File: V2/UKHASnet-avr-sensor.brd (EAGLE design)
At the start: 49.5 x 49.2 mm, 33 parts, among them J1 AVR_SPI_PRG_62X3_LOCK, U1 MCP1700-3302E/TO, U2 ATMEGA328P-PU, X1 SMA-142-0711-881/886, Y1 RESONATORPTH

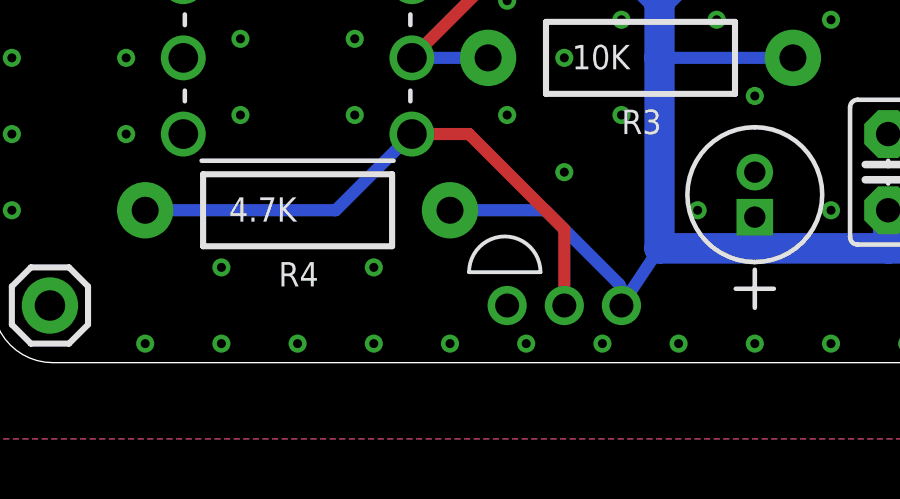
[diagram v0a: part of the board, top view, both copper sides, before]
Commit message: Add extra pad for dht22.
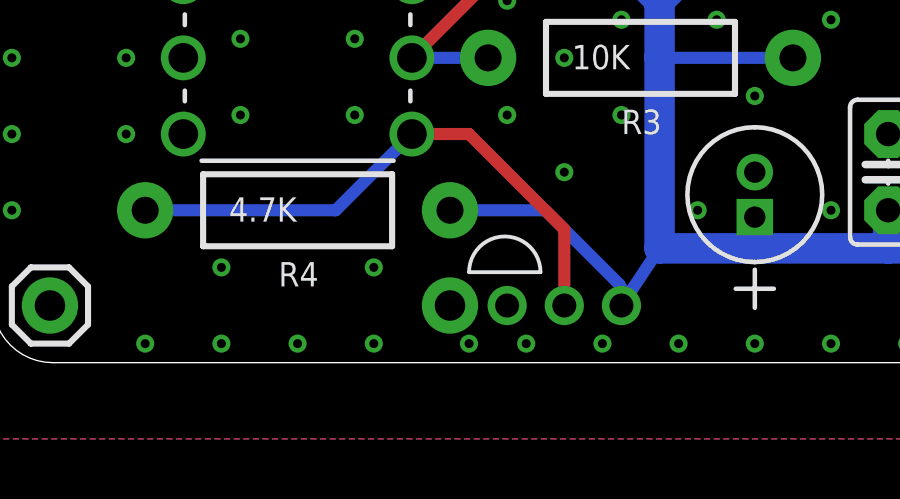
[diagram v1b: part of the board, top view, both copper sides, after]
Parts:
- added JP16: M01NOSILK-KIT, SparkFun-Connectors:1X01NS-KIT
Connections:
- net GND: now also JP16.1
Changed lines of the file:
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@@
 <layer number="54" name="bGND_GNDA" color="1" fill="9" visible="no" active="no"/>
 <layer number="56" name="wert" color="7" fill="1" visible="no" active="no"/>
+<layer number="57" name="tCAD" color="7" fill="1" visible="no" active="no"/>
 <layer number="91" name="Nets" color="2" fill="1" visible="no" active="no"/>
 <layer number="92" name="Busses" color="1" fill="1" visible="no" active="no"/>
@@
 <layer number="97" name="Info" color="7" fill="1" visible="no" active="no"/>
 <layer number="98" name="Guide" color="6" fill="1" visible="no" active="no"/>
+<layer number="99" name="SpiceOrder" color="7" fill="1" visible="no" active="no"/>
 <layer number="100" name="Muster" color="7" fill="1" visible="no" active="no"/>
 <layer number="101" name="Patch_Top" color="12" fill="4" visible="no" active="yes"/>
@@
 <layer number="109" name="fp9" color="7" fill="1" visible="no" active="yes"/>
 <layer number="110" name="fp0" color="7" fill="1" visible="no" active="yes"/>
+<layer number="111" name="LPC17xx" color="7" fill="1" visible="no" active="yes"/>
+<layer number="112" name="tSilk" color="7" fill="1" visible="no" active="yes"/>
+<layer number="113" name="IDFDebug" color="4" fill="1" visible="no" active="yes"/>
 <layer number="116" name="Patch_BOT" color="9" fill="4" visible="no" active="yes"/>
 <layer number="121" name="_tsilk" color="7" fill="1" visible="no" active="yes"/>
@@
 <layer number="124" name="bTestmark" color="7" fill="1" visible="no" active="yes"/>
 <layer number="125" name="_tNames" color="7" fill="1" visible="no" active="yes"/>
+<layer number="126" name="_bNames" color="7" fill="1" visible="no" active="yes"/>
+<layer number="127" name="_tValues" color="7" fill="1" visible="no" active="yes"/>
+<layer number="128" name="_bValues" color="7" fill="1" visible="no" active="yes"/>
 <layer number="131" name="tAdjust" color="7" fill="1" visible="no" active="yes"/>
 <layer number="132" name="bAdjust" color="7" fill="1" visible="no" active="yes"/>
 <layer number="144" name="Drill_legend" color="7" fill="1" visible="no" active="yes"/>
+<layer number="150" name="Notes" color="7" fill="1" visible="no" active="yes"/>
 <layer number="151" name="HeatSink" color="7" fill="1" visible="no" active="yes"/>
+<layer number="152" name="_bDocu" color="7" fill="1" visible="no" active="yes"/>
+<layer number="153" name="FabDoc1" color="7" fill="1" visible="no" active="yes"/>
+<layer number="154" name="FabDoc2" color="7" fill="1" visible="no" active="yes"/>
+<layer number="155" name="FabDoc3" color="7" fill="1" visible="no" active="yes"/>
 <layer number="199" name="Contour" color="7" fill="1" visible="no" active="yes"/>
 <layer number="200" name="200bmp" color="1" fill="10" visible="no" active="no"/>
@@
 <layer number="223" name="223bmp" color="24" fill="1" visible="no" active="no"/>
 <layer number="224" name="224bmp" color="25" fill="1" visible="no" active="no"/>
+<layer number="248" name="Housing" color="7" fill="1" visible="no" active="yes"/>
+<layer number="249" name="Edge" color="7" fill="1" visible="no" active="yes"/>
 <layer number="250" name="Descript" color="3" fill="1" visible="no" active="no"/>
 <layer number="251" name="SMDround" color="12" fill="11" visible="no" active="no"/>
@@
 <element name="JP15" library="SparkFun-Connectors" package="1X01" value="M01PTH" x="1.905" y="31.75" smashed="yes"/>
 <element name="U$3" library="SparkFun-Aesthetics" package="OSHW-LOGO-M" value="" x="45.72" y="8.89" rot="R90"/>
+<element name="JP16" library="SparkFun-Connectors" package="1X01NS-KIT" value="M01NOSILK-KIT" x="15.24" y="1.905"/>
 </elements>
 <signals>
@@
 <via x="10.16" y="0.635" extent="1-16" drill="0.3"/>
 <via x="12.7" y="0.635" extent="1-16" drill="0.3"/>
-<via x="15.24" y="0.635" extent="1-16" drill="0.3"/>
+<via x="15.875" y="0.635" extent="1-16" drill="0.3"/>
 <via x="17.78" y="0.635" extent="1-16" drill="0.3"/>
 <via x="20.32" y="0.635" extent="1-16" drill="0.3"/>
@@
 <via x="47.625" y="45.085" extent="1-16" drill="0.3"/>
 <via x="43.18" y="43.18" extent="1-16" drill="0.3"/>
+<contactref element="JP16" pad="1"/>
 </signal>
 <signal name="VIN">

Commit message: Fix dht22 pad.
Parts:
- removed JP16: M01NOSILK-KIT, SparkFun-Connectors:1X01NS-KIT
- added PAD1: WIREPAD1,6/0,9, wirepad:1,6/0,9
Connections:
- net GND: now also PAD1.1; no longer JP16.1
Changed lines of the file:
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@@
 <elements>
 <element name="U$1" library="hopeRF2" package="RFM" value="RFM69HW" x="47.625" y="41.91" smashed="yes" rot="R180"/>
-<element name="U$2" library="Ava" package="DS1820" value="DS1820TO92" x="16.51" y="3.175"/>
+<element name="U$2" library="Ava" package="DS1820" value="DS1820TO92" x="16.51" y="3.175" smashed="yes"/>
 <element name="J1" library="SparkFun-Connectors" package="2X3_LOCK" value="AVR_SPI_PRG_62X3_LOCK" x="44.45" y="19.05" smashed="yes" rot="R270"/>
 <element name="JP1" library="SparkFun-Connectors" package="1X02" value="M02PTH" x="47.625" y="1.905" smashed="yes" rot="R180"/>
@@
 <element name="JP15" library="SparkFun-Connectors" package="1X01" value="M01PTH" x="1.905" y="31.75" smashed="yes"/>
 <element name="U$3" library="SparkFun-Aesthetics" package="OSHW-LOGO-M" value="" x="45.72" y="8.89" rot="R90"/>
-<element name="JP16" library="SparkFun-Connectors" package="1X01NS-KIT" value="M01NOSILK-KIT" x="15.24" y="1.905"/>
+<element name="PAD1" library="wirepad" package="1,6/0,9" value="WIREPAD1,6/0,9" x="15.24" y="1.905" smashed="yes"/>
 </elements>
 <signals>
@@
 <via x="47.625" y="45.085" extent="1-16" drill="0.3"/>
 <via x="43.18" y="43.18" extent="1-16" drill="0.3"/>
-<contactref element="JP16" pad="1"/>
+<contactref element="PAD1" pad="1"/>
 </signal>
 <signal name="VIN">

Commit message: Silkscreen changes.
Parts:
- C1: value 47UF -> 47uF
- C4, C5, C6: value 100nF -> 0.1uF
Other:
- board text added: "https://ukhas.net/"
- board text removed: "http://ukhas.net/"
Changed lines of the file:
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@@
 <wire x1="2" y1="49.2" x2="0" y2="47.2" width="0" layer="20" curve="90"/>
 <text x="41.91" y="10.16" size="1.778" layer="51" distance="96" rot="R90">Phil M0DNY</text>
-<text x="24.13" y="12.7" size="1.778" layer="51" rot="R90">http://ukhas.net/</text>
+<text x="24.765" y="12.7" size="1.778" layer="51" rot="R90">https://ukhas.net/</text>
 <text x="41.91" y="1.27" size="1.9304" layer="51">+</text>
 <text x="36.83" y="10.16" size="1.778" layer="51" rot="R90">Sensor V2</text>
@@
 <element name="JP9" library="SparkFun-Connectors" package="1X01" value="M01PTH" x="24.765" y="46.355" smashed="yes"/>
 <element name="R1" library="SparkFun" package="AXIAL-0.4" value="150K" x="27.305" y="19.05" smashed="yes" rot="R90">
-<attribute name="NAME" x="26.035" y="14.605" size="0.8128" layer="25" font="vector" ratio="15" rot="R90"/>
+<attribute name="NAME" x="29.21" y="13.97" size="0.8128" layer="25" font="vector" ratio="15" rot="R90"/>
 <attribute name="VALUE" x="27.686" y="16.764" size="0.8128" layer="21" font="vector" ratio="15" rot="R90"/>
 </element>
 <element name="R2" library="SparkFun" package="AXIAL-0.4" value="470K" x="31.115" y="19.05" smashed="yes" rot="R270">
-<attribute name="NAME" x="29.21" y="15.875" size="0.8128" layer="25" font="vector" ratio="15" rot="R270"/>
+<attribute name="NAME" x="32.385" y="15.24" size="0.8128" layer="25" font="vector" ratio="15" rot="R270"/>
 <attribute name="VALUE" x="30.734" y="19.431" size="0.8128" layer="21" font="vector" ratio="15" rot="R270"/>
 </element>
@@
 <attribute name="VALUE" x="19.304" y="9.779" size="0.8128" layer="21" font="vector" ratio="15"/>
 </element>
-<element name="C1" library="1000ufCap" package="CAPPR150-400X1200" value="47UF" x="25.4" y="6.35" smashed="yes" rot="R90">
+<element name="C1" library="1000ufCap" package="CAPPR150-400X1200" value="47uF" x="25.4" y="6.35" smashed="yes" rot="R90">
 <attribute name="OC_NEWARK" value="17T5110 " x="25.4" y="6.35" size="1.778" layer="27" rot="R90" display="off"/>
 <attribute name="TOLERANCE" value="±20 %" x="25.4" y="6.35" size="1.778" layer="27" rot="R90" display="off"/>
@@
 <attribute name="SUPPLIER" value="PANASONIC " x="25.4" y="6.35" size="1.778" layer="27" rot="R90" display="off"/>
 <attribute name="OC_FARNELL" value="1848468 " x="25.4" y="6.35" size="1.778" layer="27" rot="R90" display="off"/>
+<attribute name="VALUE" x="19.7358" y="4.9784" size="0.8128" layer="27" font="vector" ratio="15" rot="SR0"/>
 </element>
 <element name="R4" library="SparkFun" package="AXIAL-0.4" value="4.7K" x="10.16" y="5.08" smashed="yes">
@@
 <element name="C2" library="capacitor-wima" package="C2.5-2" value="100nF" x="17.78" y="24.765" smashed="yes" rot="R90"/>
 <element name="C3" library="capacitor-wima" package="C2.5-2" value="100nF" x="17.78" y="29.845" smashed="yes" rot="R90"/>
-<element name="C4" library="capacitor-wima" package="C2.5-2" value="100nF" x="39.37" y="6.35" smashed="yes" rot="R90"/>
-<element name="C6" library="capacitor-wima" package="C2.5-2" value="100nF" x="29.845" y="6.35" smashed="yes" rot="R90"/>
-<element name="C5" library="capacitor-wima" package="C2.5-2" value="100nF" x="46.355" y="43.18" smashed="yes" rot="R180"/>
+<element name="C4" library="capacitor-wima" package="C2.5-2" value="0.1uF" x="39.37" y="6.35" smashed="yes" rot="R90">
+<attribute name="VALUE" x="41.021" y="3.429" size="0.8128" layer="27" font="vector" ratio="15" rot="R180"/>
+</element>
+<element name="C6" library="capacitor-wima" package="C2.5-2" value="0.1uF" x="29.845" y="6.35" smashed="yes" rot="R90">
+<attribute name="VALUE" x="31.496" y="3.429" size="0.8128" layer="27" font="vector" ratio="15" rot="R180"/>
+</element>
+<element name="C5" library="capacitor-wima" package="C2.5-2" value="0.1uF" x="46.355" y="43.18" smashed="yes" rot="R180">
+<attribute name="VALUE" x="46.736" y="45.974" size="0.8128" layer="27" font="vector" ratio="15" rot="R180"/>
+</element>
 <element name="JP5" library="SparkFun-Connectors" package="1X01" value="M01PTH" x="1.905" y="28.575" smashed="yes"/>
 <element name="JP6" library="SparkFun-Connectors" package="1X01" value="M01PTH" x="1.905" y="26.035" smashed="yes"/>

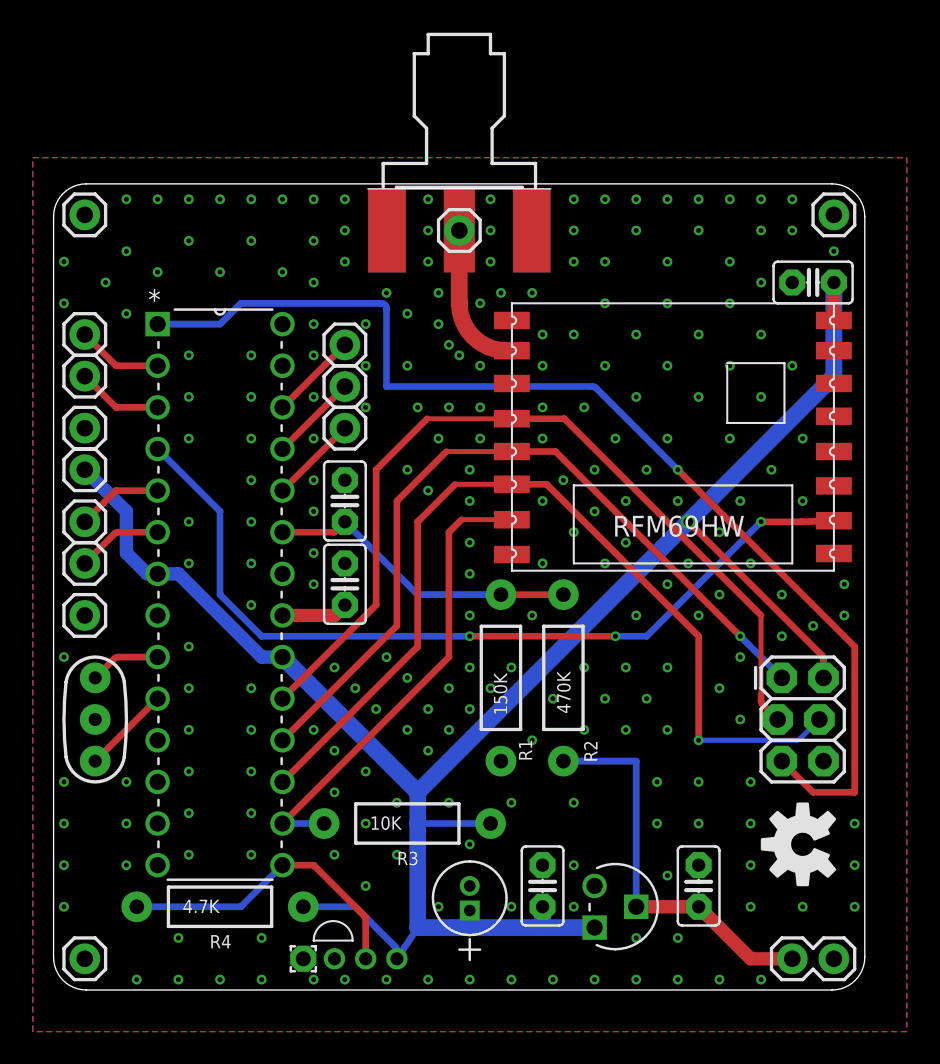
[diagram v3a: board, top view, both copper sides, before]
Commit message: Silkscreen changes.
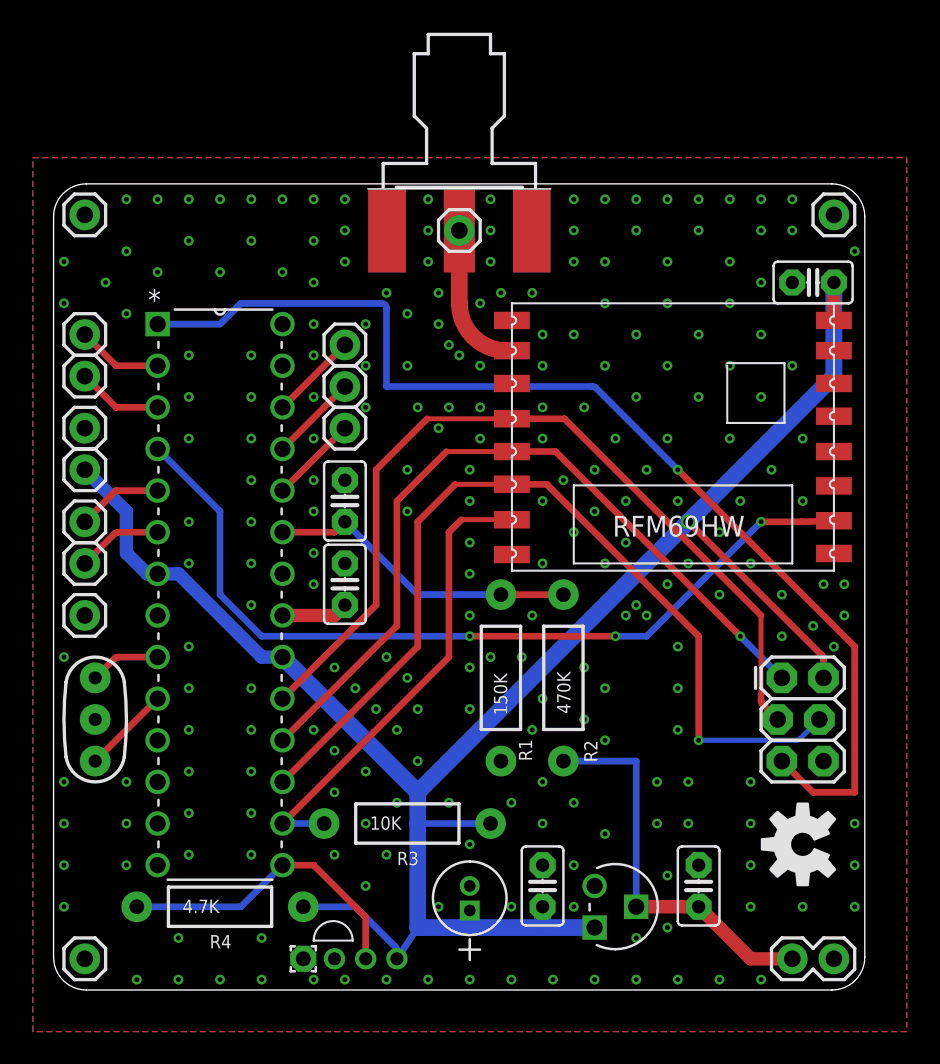
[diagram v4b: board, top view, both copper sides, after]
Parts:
- C2, C3: value 100nF -> 0.1uF
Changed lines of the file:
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@@
 <element name="JP13" library="SparkFun-Connectors" package="1X01" value="M01PTH" x="1.905" y="37.465" smashed="yes"/>
 <element name="JP14" library="SparkFun-Connectors" package="1X01" value="M01PTH" x="1.905" y="40.005" smashed="yes"/>
-<element name="C2" library="capacitor-wima" package="C2.5-2" value="100nF" x="17.78" y="24.765" smashed="yes" rot="R90"/>
-<element name="C3" library="capacitor-wima" package="C2.5-2" value="100nF" x="17.78" y="29.845" smashed="yes" rot="R90"/>
+<element name="C2" library="capacitor-wima" package="C2.5-2" value="0.1uF" x="17.78" y="24.765" smashed="yes" rot="R90">
+<attribute name="VALUE" x="20.574" y="23.114" size="0.8128" layer="27" font="vector" ratio="15" rot="R90"/>
+</element>
+<element name="C3" library="capacitor-wima" package="C2.5-2" value="0.1uF" x="17.78" y="29.845" smashed="yes" rot="R90">
+<attribute name="VALUE" x="20.574" y="28.194" size="0.8128" layer="27" font="vector" ratio="15" rot="R90"/>
+</element>
 <element name="C4" library="capacitor-wima" package="C2.5-2" value="0.1uF" x="39.37" y="6.35" smashed="yes" rot="R90">
 <attribute name="VALUE" x="41.021" y="3.429" size="0.8128" layer="27" font="vector" ratio="15" rot="R180"/>
@@
 </element>
 <element name="C5" library="capacitor-wima" package="C2.5-2" value="0.1uF" x="46.355" y="43.18" smashed="yes" rot="R180">
-<attribute name="VALUE" x="46.736" y="45.974" size="0.8128" layer="27" font="vector" ratio="15" rot="R180"/>
+<attribute name="VALUE" x="44.704" y="44.831" size="0.8128" layer="27" font="vector" ratio="15"/>
 </element>
 <element name="JP5" library="SparkFun-Connectors" package="1X01" value="M01PTH" x="1.905" y="28.575" smashed="yes"/>
@@
 <via x="48.895" y="7.62" extent="1-16" drill="0.3"/>
 <via x="48.895" y="10.16" extent="1-16" drill="0.3"/>
-<via x="38.1" y="3.175" extent="1-16" drill="0.3"/>
+<via x="37.465" y="3.81" extent="1-16" drill="0.3"/>
 <via x="35.56" y="3.175" extent="1-16" drill="0.3"/>
 <via x="37.465" y="6.985" extent="1-16" drill="0.3"/>
@@
 <via x="17.145" y="8.255" extent="1-16" drill="0.3"/>
 <via x="19.05" y="6.35" extent="1-16" drill="0.3"/>
-<via x="20.955" y="8.255" extent="1-16" drill="0.3"/>
+<via x="20.32" y="8.255" extent="1-16" drill="0.3"/>
 <via x="19.05" y="10.16" extent="1-16" drill="0.3"/>
 <via x="17.145" y="14.605" extent="1-16" drill="0.3"/>
@@
 <via x="20.32" y="20.32" extent="1-16" drill="0.3"/>
 <via x="21.59" y="31.75" extent="1-16" drill="0.3"/>
-<via x="22.86" y="30.48" extent="1-16" drill="0.3"/>
+<via x="21.59" y="29.21" extent="1-16" drill="0.3"/>
 <via x="15.875" y="26.67" extent="1-16" drill="0.3"/>
 <via x="15.875" y="29.21" extent="1-16" drill="0.3"/>
@@
 <via x="25.4" y="27.305" extent="1-16" drill="0.3"/>
 <via x="37.465" y="24.765" extent="1-16" drill="0.3"/>
-<via x="35.56" y="22.86" extent="1-16" drill="0.3"/>
+<via x="35.56" y="23.495" extent="1-16" drill="0.3"/>
 <via x="25.4" y="19.685" extent="1-16" drill="0.3"/>
-<via x="24.13" y="18.415" extent="1-16" drill="0.3"/>
-<via x="22.86" y="17.145" extent="1-16" drill="0.3"/>
-<via x="21.59" y="15.875" extent="1-16" drill="0.3"/>
-<via x="22.86" y="14.605" extent="1-16" drill="0.3"/>
-<via x="24.13" y="15.875" extent="1-16" drill="0.3"/>
+<via x="29.845" y="12.7" extent="1-16" drill="0.3"/>
+<via x="22.225" y="17.145" extent="1-16" drill="0.3"/>
+<via x="20.955" y="15.875" extent="1-16" drill="0.3"/>
+<via x="22.225" y="13.97" extent="1-16" drill="0.3"/>
+<via x="33.655" y="9.525" extent="1-16" drill="0.3"/>
 <via x="25.4" y="17.145" extent="1-16" drill="0.3"/>
-<via x="26.67" y="18.415" extent="1-16" drill="0.3"/>
-<via x="27.94" y="19.685" extent="1-16" drill="0.3"/>
+<via x="26.67" y="20.32" extent="1-16" drill="0.3"/>
+<via x="28.575" y="20.32" extent="1-16" drill="0.3"/>
 <via x="29.21" y="22.86" extent="1-16" drill="0.3"/>
-<via x="29.21" y="15.24" extent="1-16" drill="0.3"/>
-<via x="30.48" y="17.78" extent="1-16" drill="0.3"/>
+<via x="29.21" y="15.875" extent="1-16" drill="0.3"/>
+<via x="29.845" y="17.78" extent="1-16" drill="0.3"/>
 <via x="32.385" y="19.685" extent="1-16" drill="0.3"/>
-<via x="34.925" y="19.685" extent="1-16" drill="0.3"/>
-<via x="33.655" y="17.78" extent="1-16" drill="0.3"/>
-<via x="32.385" y="15.875" extent="1-16" drill="0.3"/>
-<via x="34.925" y="15.875" extent="1-16" drill="0.3"/>
+<via x="34.925" y="22.86" extent="1-16" drill="0.3"/>
+<via x="33.655" y="18.415" extent="1-16" drill="0.3"/>
+<via x="32.385" y="16.51" extent="1-16" drill="0.3"/>
+<via x="38.1" y="20.955" extent="1-16" drill="0.3"/>
 <via x="42.545" y="10.16" extent="1-16" drill="0.3"/>
 <via x="42.545" y="7.62" extent="1-16" drill="0.3"/>
 <via x="45.72" y="5.08" extent="1-16" drill="0.3"/>
 <via x="42.545" y="5.08" extent="1-16" drill="0.3"/>
-<via x="39.37" y="10.16" extent="1-16" drill="0.3"/>
-<via x="39.37" y="12.7" extent="1-16" drill="0.3"/>
+<via x="38.735" y="10.16" extent="1-16" drill="0.3"/>
+<via x="38.735" y="12.7" extent="1-16" drill="0.3"/>
 <via x="42.545" y="12.7" extent="1-16" drill="0.3"/>
 <via x="36.83" y="10.16" extent="1-16" drill="0.3"/>
-<via x="37.465" y="15.875" extent="1-16" drill="0.3"/>
-<via x="37.465" y="19.685" extent="1-16" drill="0.3"/>
-<via x="36.195" y="17.78" extent="1-16" drill="0.3"/>
-<via x="39.37" y="22.86" extent="1-16" drill="0.3"/>
-<via x="41.91" y="20.32" extent="1-16" drill="0.3"/>
-<via x="40.64" y="18.415" extent="1-16" drill="0.3"/>
-<via x="41.91" y="16.51" extent="1-16" drill="0.3"/>
+<via x="38.1" y="15.875" extent="1-16" drill="0.3"/>
+<via x="38.1" y="18.415" extent="1-16" drill="0.3"/>
+<via x="33.655" y="15.24" extent="1-16" drill="0.3"/>
+<via x="36.195" y="22.86" extent="1-16" drill="0.3"/>
+<via x="47.625" y="20.955" extent="1-16" drill="0.3"/>
+<via x="29.845" y="10.16" extent="1-16" drill="0.3"/>
+<via x="46.99" y="24.765" extent="1-16" drill="0.3"/>
 <via x="40.64" y="27.94" extent="1-16" drill="0.3"/>
 <via x="42.545" y="26.035" extent="1-16" drill="0.3"/>
@@
 <via x="29.845" y="33.655" extent="1-16" drill="0.3"/>
 <via x="26.035" y="33.655" extent="1-16" drill="0.3"/>
-<via x="23.495" y="33.655" extent="1-16" drill="0.3"/>
+<via x="23.495" y="34.29" extent="1-16" drill="0.3"/>
 <via x="33.02" y="31.75" extent="1-16" drill="0.3"/>
 <via x="34.925" y="29.845" extent="1-16" drill="0.3"/>
@@
 <via x="25.4" y="25.4" extent="1-16" drill="0.3"/>
 <via x="45.085" y="46.355" extent="1-16" drill="0.3"/>
-<via x="47.625" y="45.085" extent="1-16" drill="0.3"/>
+<via x="48.895" y="45.085" extent="1-16" drill="0.3"/>
 <via x="43.18" y="43.18" extent="1-16" drill="0.3"/>
 <contactref element="PAD1" pad="1"/>
